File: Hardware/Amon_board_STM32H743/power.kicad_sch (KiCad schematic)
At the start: 91 parts, among them J16 XT60PW-M20, J17 XT60PW-M20, Q6 BC817, Q7 AO3401A, Q8 BC817, Q9 AO3401A, U15 MP2303ADN, U4 MP2303ADN, U5 MP2303ADN

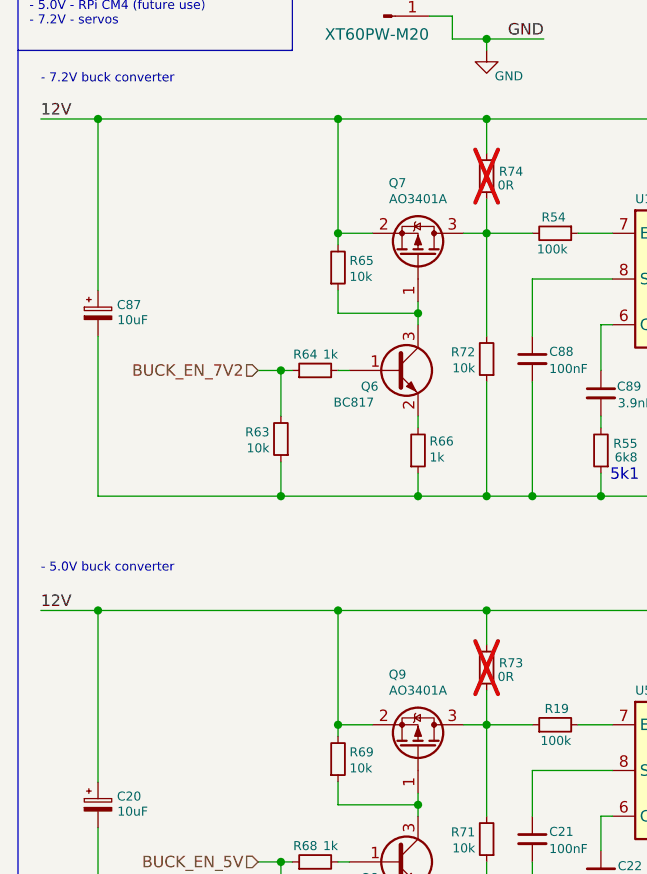
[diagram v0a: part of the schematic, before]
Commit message: Update: finished PCB v3, gerbers, ordered board, readme update
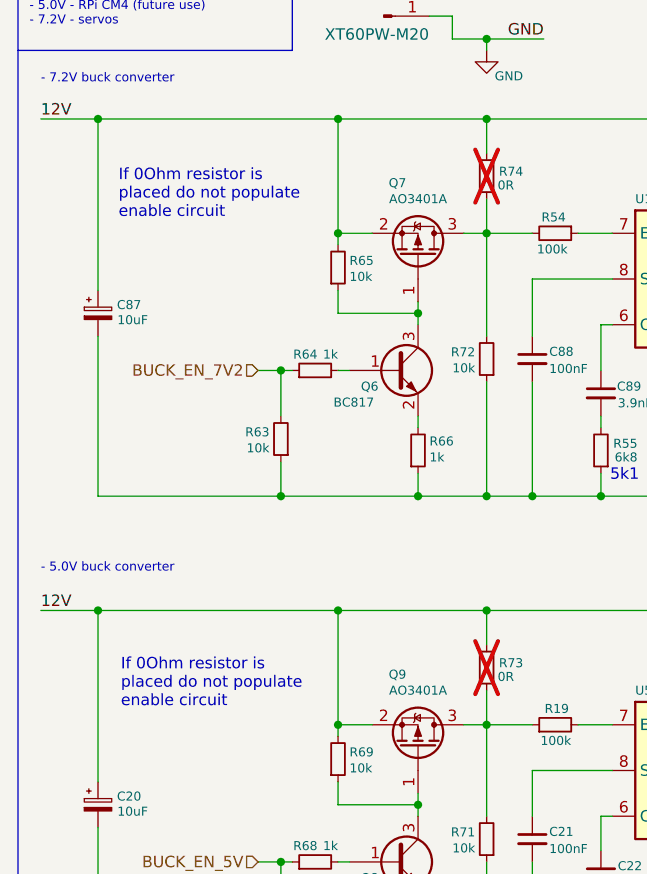
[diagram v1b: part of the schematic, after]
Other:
- note added: "If 0Ohm resistor is placed do not populate enable circuit"
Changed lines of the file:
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@@
 				(bold yes)
 				(italic yes)
+				(color 132 0 0 1)
 			)
 			(justify left bottom)
@@
 		)
 	)
+	(text "If 0Ohm resistor is \nplaced do not populate \nenable circuit"
+		(exclude_from_sim no)
+		(at 26.67 102.362 0)
+		(effects
+			(font
+				(size 1.27 1.27)
+			)
+			(justify left bottom)
+		)
+	)
 	(text "12V battery to:\n- 3.3V - mcu, sensors...\n- 5.0V - RPi CM4 (future use)\n- 7.2V - servos\n\n"
 		(exclude_from_sim no)
@@
 		)
 	)
+	(text "If 0Ohm resistor is \nplaced do not populate \nenable circuit"
+		(exclude_from_sim no)
+		(at 26.416 48.006 0)
+		(effects
+			(font
+				(size 1.27 1.27)
+			)
+			(justify left bottom)
+		)
+	)
 	(text "EDF BAT. SENSE:"
 		(exclude_from_sim no)
@@
 				(bold yes)
 				(italic yes)
+				(color 132 0 0 1)
 			)
 			(justify left bottom)
@@
 				(bold yes)
 				(italic yes)
+				(color 132 0 0 1)
 			)
 			(justify left bottom)

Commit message: Update: PCB bringup in progress, some modifications done, fw in development
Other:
- note added: "3.3nF"
- note added: "51k||51k"
- note added: "57k"
- note removed: "5k1||5k1"

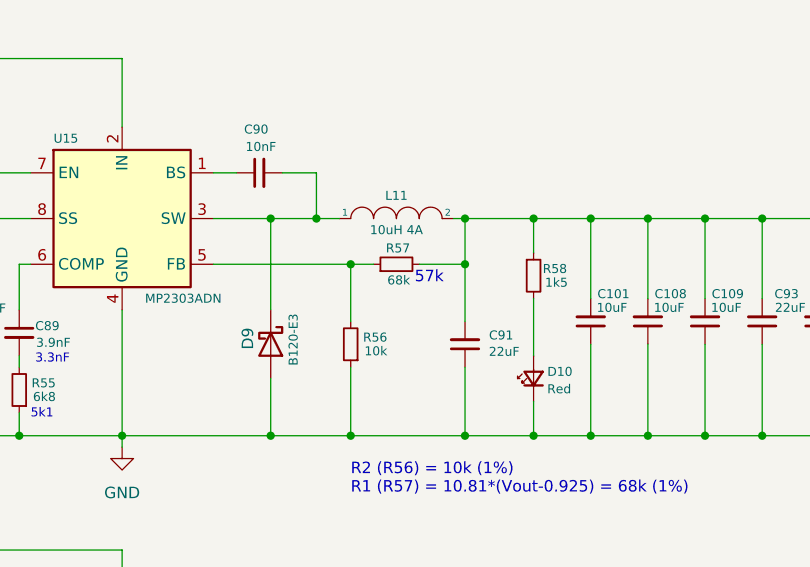
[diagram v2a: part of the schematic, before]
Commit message: Update: full FW port to PCB_v3 with all SPI problems solved, corrected timers, untested on craft
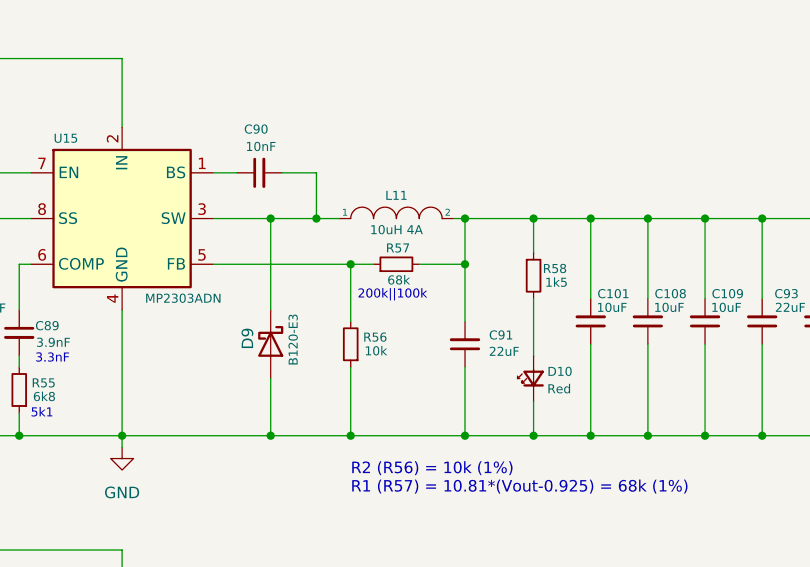
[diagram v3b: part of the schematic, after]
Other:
- note added: "200k||100k"
- note removed: "57k"
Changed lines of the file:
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@@
 		)
 	)
-	(text "57k"
+	(text "200k||100k"
 		(exclude_from_sim no)
-		(at 123.952 61.976 0)
+		(at 117.602 63.754 0)
 		(effects
 			(font
-				(size 1.27 1.27)
+				(size 1 1)
 			)
 			(justify left bottom)
